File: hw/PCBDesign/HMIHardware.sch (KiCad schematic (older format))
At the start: 8 parts, among them U1 74HC165, U2 74HC165, U3 74HC165

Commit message: Added PCB
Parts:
- added R45, R46, R47, R49, R51: 10k, Resistor_SMD:R_0402_1005Metric, symbol Device:R_US
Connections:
- net GND: now also R45.2, R46.2, R47.2, R49.2, R51.2
- net d22: now also R45.1
- net d4: now also R46.1
- net d5: now also R47.1
- net d6: now also R49.1
- net d7: now also R51.1
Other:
- moved on the sheet: R2
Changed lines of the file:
@@
 F1 "ButtonInput.sch" 50
 F2 "V+" I L 9600 1750 50
-F3 "KeyLeft" O L 9600 1900 50
-F4 "KeyRight" O L 9600 2000 50
-F5 "KeyUp" O L 9600 2100 50
-F6 "KeyDown" O L 9600 2200 50
-F7 "KeyEnter" O L 9600 2300 50
-F8 "KeyEscape" O L 9600 2400 50
-F9 "KeyReset" O L 9600 2500 50
-F10 "KeyBoot" O L 9600 2600 50
+F3 "KeyReset" O L 9600 2500 50
+F4 "KeyBoot" O L 9600 2000 50
+F5 "KeyUser" O L 9600 1900 50
 $EndSheet
 Text HLabel 9550 6000 0    50   Input ~ 0
@@
 Wire Wire Line
 	9600 2000 9200 2000
-Wire Wire Line
-	9600 2100 9200 2100
-Wire Wire Line
-	9600 2200 9200 2200
-Wire Wire Line
-	9600 2300 9200 2300
-Wire Wire Line
-	9600 2400 9200 2400
 Wire Bus Line
 	7250 2800 9100 2800
@@
 Entry Wire Line
 	9100 1900 9200 2000
-Entry Wire Line
-	9100 2000 9200 2100
-Entry Wire Line
-	9100 2100 9200 2200
-Entry Wire Line
-	9100 2200 9200 2300
-Entry Wire Line
-	9100 2300 9200 2400
 Text Label 7000 2000 0    50   ~ 0
 d0
@@
 Text Label 9300 2000 0    50   ~ 0
 d3
-Text Label 9300 2100 0    50   ~ 0
-d4
-Text Label 9300 2200 0    50   ~ 0
-d5
-Text Label 9300 2300 0    50   ~ 0
-d6
-Text Label 9300 2400 0    50   ~ 0
-d7
 Wire Wire Line
 	4900 2000 5100 2000
@@
 L Device:R_US R2
 U 1 1 60588674
-P 8400 4650
-F 0 "R2" H 8468 4696 50  0000 L CNN
-F 1 "10k" H 8468 4605 50  0000 L CNN
-F 2 "Resistor_SMD:R_0402_1005Metric" V 8440 4640 50  0001 C CNN
-F 3 "~" H 8400 4650 50  0001 C CNN
-F 4 "C25744" H 8400 4650 50  0001 C CNN "LCSC"
-	1    8400 4650
+P 5250 4650
+F 0 "R2" H 5318 4696 50  0000 L CNN
+F 1 "10k" H 5318 4605 50  0000 L CNN
+F 2 "Resistor_SMD:R_0402_1005Metric" V 5290 4640 50  0001 C CNN
+F 3 "~" H 5250 4650 50  0001 C CNN
+F 4 "C25744" H 5250 4650 50  0001 C CNN "LCSC"
+	1    5250 4650
 	1    0    0    -1
 $EndComp
@@
 L power:GND #PWR020
 U 1 1 60589A9A
-P 8400 4800
-F 0 "#PWR020" H 8400 4550 50  0001 C CNN
-F 1 "GND" H 8405 4627 50  0000 C CNN
-F 2 "" H 8400 4800 50  0001 C CNN
-F 3 "" H 8400 4800 50  0001 C CNN
-	1    8400 4800
-	1    0    0    -1
-$EndComp
-Entry Wire Line
-	7400 4250 7500 4350
-Entry Wire Line
-	7700 4250 7800 4350
-Entry Wire Line
-	8000 4250 8100 4350
-Entry Wire Line
-	8300 4250 8400 4350
-Wire Wire Line
-	8400 4500 8400 4350
-Wire Wire Line
-	7800 4500 7800 4350
-Wire Wire Line
-	7500 4500 7500 4350
-Text Label 7500 4400 0    50   ~ 0
+P 5250 4800
+F 0 "#PWR020" H 5250 4550 50  0001 C CNN
+F 1 "GND" H 5255 4627 50  0000 C CNN
+F 2 "" H 5250 4800 50  0001 C CNN
+F 3 "" H 5250 4800 50  0001 C CNN
+	1    5250 4800
+	1    0    0    -1
+$EndComp
+Entry Wire Line
+	4250 4250 4350 4350
+Entry Wire Line
+	4550 4250 4650 4350
+Entry Wire Line
+	4850 4250 4950 4350
+Entry Wire Line
+	5150 4250 5250 4350
+Wire Wire Line
+	5250 4500 5250 4350
+Wire Wire Line
+	4650 4500 4650 4350
+Wire Wire Line
+	4350 4500 4350 4350
+Text Label 4350 4400 0    50   ~ 0
 d20
-Text Label 7800 4400 0    50   ~ 0
+Text Label 4650 4400 0    50   ~ 0
 d21
-Text Label 8100 4400 0    50   ~ 0
+Text Label 4950 4400 0    50   ~ 0
 d22
-Text Label 8400 4400 0    50   ~ 0
+Text Label 5250 4400 0    50   ~ 0
 d23
-Text Notes 8700 5550 1    50   ~ 0
+Text Notes 6300 5150 2    50   ~ 0
 These inputs currently unused
-Text GLabel 7500 4500 3    50   Output ~ 0
+Text GLabel 4350 4500 3    50   Output ~ 0
 nBatteryPowerGood
-Text GLabel 7800 4500 3    50   Output ~ 0
+Text GLabel 4650 4500 3    50   Output ~ 0
 nBatteryChargeGood
-Wire Wire Line
-	9200 2600 9600 2600
-Text Label 9200 2600 0    50   ~ 0
-nBoot
-Wire Wire Line
-	8100 4350 8100 4900
+$Comp
+L Device:R_US R45
+U 1 1 604B372E
+P 4950 4650
+F 0 "R45" H 5018 4696 50  0000 L CNN
+F 1 "10k" H 5018 4605 50  0000 L CNN
+F 2 "Resistor_SMD:R_0402_1005Metric" V 4990 4640 50  0001 C CNN
+F 3 "~" H 4950 4650 50  0001 C CNN
+F 4 "C25744" H 4950 4650 50  0001 C CNN "LCSC"
+	1    4950 4650
+	1    0    0    -1
+$EndComp
+$Comp
+L power:GND #PWR056
+U 1 1 604B3734
+P 4950 4800
+F 0 "#PWR056" H 4950 4550 50  0001 C CNN
+F 1 "GND" H 4955 4627 50  0000 C CNN
+F 2 "" H 4950 4800 50  0001 C CNN
+F 3 "" H 4950 4800 50  0001 C CNN
+	1    4950 4800
+	1    0    0    -1
+$EndComp
+Wire Wire Line
+	4950 4500 4950 4350
+$Comp
+L Device:R_US R46
+U 1 1 604BF334
+P 5550 4650
+F 0 "R46" H 5618 4696 50  0000 L CNN
+F 1 "10k" H 5618 4605 50  0000 L CNN
+F 2 "Resistor_SMD:R_0402_1005Metric" V 5590 4640 50  0001 C CNN
+F 3 "~" H 5550 4650 50  0001 C CNN
+F 4 "C25744" H 5550 4650 50  0001 C CNN "LCSC"
+	1    5550 4650
+	1    0    0    -1
+$EndComp
+$Comp
+L power:GND #PWR057
+U 1 1 604BF33A
+P 5550 4800
+F 0 "#PWR057" H 5550 4550 50  0001 C CNN
+F 1 "GND" H 5555 4627 50  0000 C CNN
+F 2 "" H 5550 4800 50  0001 C CNN
+F 3 "" H 5550 4800 50  0001 C CNN
+	1    5550 4800
+	1    0    0    -1
+$EndComp
+Entry Wire Line
+	5450 4250 5550 4350
+Wire Wire Line
+	5550 4500 5550 4350
+Text Label 5550 4400 0    50   ~ 0
+d4
+$Comp
+L Device:R_US R47
+U 1 1 604C2A2C
+P 5850 4650
+F 0 "R47" H 5918 4696 50  0000 L CNN
+F 1 "10k" H 5918 4605 50  0000 L CNN
+F 2 "Resistor_SMD:R_0402_1005Metric" V 5890 4640 50  0001 C CNN
+F 3 "~" H 5850 4650 50  0001 C CNN
+F 4 "C25744" H 5850 4650 50  0001 C CNN "LCSC"
+	1    5850 4650
+	1    0    0    -1
+$EndComp
+$Comp
+L power:GND #PWR058
+U 1 1 604C2A32
+P 5850 4800
+F 0 "#PWR058" H 5850 4550 50  0001 C CNN
+F 1 "GND" H 5855 4627 50  0000 C CNN
+F 2 "" H 5850 4800 50  0001 C CNN
+F 3 "" H 5850 4800 50  0001 C CNN
+	1    5850 4800
+	1    0    0    -1
+$EndComp
+Entry Wire Line
+	5750 4250 5850 4350
+Wire Wire Line
+	5850 4500 5850 4350
+Text Label 5850 4400 0    50   ~ 0
+d5
+$Comp
+L Device:R_US R49
+U 1 1 604C6290
+P 6150 4650
+F 0 "R49" H 6218 4696 50  0000 L CNN
+F 1 "10k" H 6218 4605 50  0000 L CNN
+F 2 "Resistor_SMD:R_0402_1005Metric" V 6190 4640 50  0001 C CNN
+F 3 "~" H 6150 4650 50  0001 C CNN
+F 4 "C25744" H 6150 4650 50  0001 C CNN "LCSC"
+	1    6150 4650
+	1    0    0    -1
+$EndComp
+$Comp
+L power:GND #PWR060
+U 1 1 604C6296
+P 6150 4800
+F 0 "#PWR060" H 6150 4550 50  0001 C CNN
+F 1 "GND" H 6155 4627 50  0000 C CNN
+F 2 "" H 6150 4800 50  0001 C CNN
+F 3 "" H 6150 4800 50  0001 C CNN
+	1    6150 4800
+	1    0    0    -1
+$EndComp
+Entry Wire Line
+	6050 4250 6150 4350
+Wire Wire Line
+	6150 4500 6150 4350
+Text Label 6150 4400 0    50   ~ 0
+d6
+$Comp
+L Device:R_US R51
+U 1 1 604C9E66
+P 6450 4650
+F 0 "R51" H 6518 4696 50  0000 L CNN
+F 1 "10k" H 6518 4605 50  0000 L CNN
+F 2 "Resistor_SMD:R_0402_1005Metric" V 6490 4640 50  0001 C CNN
+F 3 "~" H 6450 4650 50  0001 C CNN
+F 4 "C25744" H 6450 4650 50  0001 C CNN "LCSC"
+	1    6450 4650
+	1    0    0    -1
+$EndComp
+$Comp
+L power:GND #PWR062
+U 1 1 604C9E6C
+P 6450 4800
+F 0 "#PWR062" H 6450 4550 50  0001 C CNN
+F 1 "GND" H 6455 4627 50  0000 C CNN
+F 2 "" H 6450 4800 50  0001 C CNN
+F 3 "" H 6450 4800 50  0001 C CNN
+	1    6450 4800
+	1    0    0    -1
+$EndComp
+Entry Wire Line
+	6350 4250 6450 4350
+Wire Wire Line
+	6450 4500 6450 4350
+Text Label 6450 4400 0    50   ~ 0
+d7
 Wire Bus Line
 	9100 3950 9100 4250
 Wire Bus Line
+	9100 900  9100 2800
+Wire Bus Line
+	7250 2100 7250 2800
+Wire Bus Line
+	5200 2100 5200 2800
+Wire Bus Line
+	9100 3100 9100 3800
+Wire Bus Line
+	3000 2100 3000 2800
+Wire Bus Line
 	3500 4250 9100 4250
-Wire Bus Line
-	7250 2100 7250 2800
-Wire Bus Line
-	5200 2100 5200 2800
-Wire Bus Line
-	9100 3100 9100 3800
-Wire Bus Line
-	3000 2100 3000 2800
-Wire Bus Line
-	9100 900  9100 2800
-Text Label 8100 4900 1    50   ~ 0
-nBoot
 $EndSCHEMATC

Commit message: Lay out more PCB
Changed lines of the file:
@@
 Wire Wire Line
 	9600 2000 9200 2000
-Wire Bus Line
-	7250 2800 9100 2800
-Entry Wire Line
-	9100 900  9200 1000
-Entry Wire Line
-	9100 1000 9200 1100
-Entry Wire Line
-	9100 1800 9200 1900
-Entry Wire Line
-	9100 1900 9200 2000
 Text Label 7000 2000 0    50   ~ 0
 d0
@@
 Text Label 7000 2700 0    50   ~ 0
 d7
-Text Label 9300 1000 0    50   ~ 0
-d0
-Text Label 9300 1100 0    50   ~ 0
-d1
-Text Label 9300 1900 0    50   ~ 0
-d2
-Text Label 9300 2000 0    50   ~ 0
-d3
 Wire Wire Line
 	4900 2000 5100 2000
@@
 Entry Wire Line
 	9100 3800 9200 3900
-Wire Bus Line
-	5200 2800 5650 2800
 Text Label 4950 2000 0    50   ~ 0
 d8
@@
 Text Label 4950 2700 0    50   ~ 0
 d15
-Text Label 9300 3200 0    50   ~ 0
-d8
-Text Label 9300 3300 0    50   ~ 0
-d9
-Text Label 9300 3400 0    50   ~ 0
-d10
-Text Label 9300 3500 0    50   ~ 0
-d11
-Text Label 9300 3600 0    50   ~ 0
-d12
-Text Label 9300 3700 0    50   ~ 0
-d13
-Text Label 9300 3800 0    50   ~ 0
-d14
-Text Label 9300 3900 0    50   ~ 0
-d15
-Wire Bus Line
-	9100 3800 5650 3800
-Wire Bus Line
-	5650 2800 5650 3800
 Entry Wire Line
 	9100 3950 9200 4050
@@
 Entry Wire Line
 	9100 4250 9200 4350
-Text Label 9300 4050 0    50   ~ 0
-d16
-Text Label 9300 4150 0    50   ~ 0
-d17
-Text Label 9300 4250 0    50   ~ 0
-d18
-Text Label 9300 4350 0    50   ~ 0
-d19
 Wire Wire Line
 	2700 2000 2900 2000
@@
 Entry Wire Line
 	2900 2300 3000 2400
-Wire Bus Line
-	3000 2800 3500 2800
-Wire Bus Line
-	3500 2800 3500 4250
 Text Label 2750 2000 0    50   ~ 0
 d16
@@
 Wire Wire Line
 	4350 4500 4350 4350
-Text Label 4350 4400 0    50   ~ 0
-d20
-Text Label 4650 4400 0    50   ~ 0
-d21
-Text Label 4950 4400 0    50   ~ 0
-d22
-Text Label 5250 4400 0    50   ~ 0
-d23
 Text Notes 6300 5150 2    50   ~ 0
 These inputs currently unused
@@
 Wire Wire Line
 	5550 4500 5550 4350
-Text Label 5550 4400 0    50   ~ 0
-d4
 $Comp
 L Device:R_US R47
@@
 Wire Wire Line
 	5850 4500 5850 4350
-Text Label 5850 4400 0    50   ~ 0
-d5
 $Comp
 L Device:R_US R49
@@
 Wire Wire Line
 	6150 4500 6150 4350
-Text Label 6150 4400 0    50   ~ 0
-d6
 $Comp
 L Device:R_US R51
@@
 Wire Wire Line
 	6450 4500 6450 4350
-Text Label 6450 4400 0    50   ~ 0
-d7
-Wire Bus Line
-	9100 3950 9100 4250
-Wire Bus Line
-	9100 900  9100 2800
 Wire Bus Line
 	7250 2100 7250 2800
@@
 	5200 2100 5200 2800
 Wire Bus Line
-	9100 3100 9100 3800
-Wire Bus Line
 	3000 2100 3000 2800
-Wire Bus Line
-	3500 4250 9100 4250
 $EndSCHEMATC

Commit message: Complete route of draft #1 finished
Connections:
- wire segments 77 -> 75
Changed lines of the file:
@@
 Wire Wire Line
 	9500 2500 9600 2500
-Text HLabel 9500 4800 0    50   Input ~ 0
-VAnalogRef
 Wire Wire Line
 	9500 5050 9600 5050
@@
 Wire Wire Line
 	6950 2700 7150 2700
-Entry Wire Line
-	7150 2000 7250 2100
-Entry Wire Line
-	7150 2100 7250 2200
-Entry Wire Line
-	7150 2200 7250 2300
-Entry Wire Line
-	7150 2300 7250 2400
-Entry Wire Line
-	7150 2400 7250 2500
-Entry Wire Line
-	7150 2500 7250 2600
-Entry Wire Line
-	7150 2600 7250 2700
-Entry Wire Line
-	7150 2700 7250 2800
 Wire Wire Line
 	9600 1000 9200 1000
@@
 Wire Wire Line
 	4900 2700 5100 2700
-Entry Wire Line
-	5100 2000 5200 2100
-Entry Wire Line
-	5100 2100 5200 2200
-Entry Wire Line
-	5100 2200 5200 2300
-Entry Wire Line
-	5100 2300 5200 2400
-Entry Wire Line
-	5100 2400 5200 2500
-Entry Wire Line
-	5100 2500 5200 2600
-Entry Wire Line
-	5100 2600 5200 2700
-Entry Wire Line
-	5100 2700 5200 2800
 Wire Wire Line
 	9600 3200 9200 3200
@@
 Wire Wire Line
 	9600 4350 9200 4350
-Entry Wire Line
-	9100 3100 9200 3200
-Entry Wire Line
-	9100 3300 9200 3400
-Entry Wire Line
-	9100 3200 9200 3300
-Entry Wire Line
-	9100 3400 9200 3500
-Entry Wire Line
-	9100 3600 9200 3700
-Entry Wire Line
-	9100 3700 9200 3800
-Entry Wire Line
-	9100 3500 9200 3600
-Entry Wire Line
-	9100 3800 9200 3900
 Text Label 4950 2000 0    50   ~ 0
 d8
@@
 Text Label 4950 2700 0    50   ~ 0
 d15
-Entry Wire Line
-	9100 3950 9200 4050
-Entry Wire Line
-	9100 4050 9200 4150
-Entry Wire Line
-	9100 4150 9200 4250
-Entry Wire Line
-	9100 4250 9200 4350
 Wire Wire Line
 	2700 2000 2900 2000
@@
 Wire Wire Line
 	2700 2700 2900 2700
-Entry Wire Line
-	2900 2000 3000 2100
-Entry Wire Line
-	2900 2100 3000 2200
-Entry Wire Line
-	2900 2200 3000 2300
-Entry Wire Line
-	2900 2300 3000 2400
 Text Label 2750 2000 0    50   ~ 0
 d16
@@
 Text Label 2750 2700 0    50   ~ 0
 d23
-Entry Wire Line
-	2900 2700 3000 2800
-Entry Wire Line
-	2900 2600 3000 2700
-Entry Wire Line
-	2900 2500 3000 2600
-Entry Wire Line
-	2900 2400 3000 2500
 $Comp
 L Device:R_US R2
@@
 	1    0    0    -1
 $EndComp
-Entry Wire Line
-	4250 4250 4350 4350
-Entry Wire Line
-	4550 4250 4650 4350
-Entry Wire Line
-	4850 4250 4950 4350
-Entry Wire Line
-	5150 4250 5250 4350
 Wire Wire Line
 	5250 4500 5250 4350
-Wire Wire Line
-	4650 4500 4650 4350
-Wire Wire Line
-	4350 4500 4350 4350
 Text Notes 6300 5150 2    50   ~ 0
 These inputs currently unused
-Text GLabel 4350 4500 3    50   Output ~ 0
+Text GLabel 7150 2000 2    50   Output ~ 0
 nBatteryPowerGood
-Text GLabel 4650 4500 3    50   Output ~ 0
+Text GLabel 7150 2100 2    50   Output ~ 0
 nBatteryChargeGood
 $Comp
@@
 	1    0    0    -1
 $EndComp
-Entry Wire Line
-	5450 4250 5550 4350
 Wire Wire Line
 	5550 4500 5550 4350
@@
 	1    0    0    -1
 $EndComp
-Entry Wire Line
-	5750 4250 5850 4350
 Wire Wire Line
 	5850 4500 5850 4350
@@
 	1    0    0    -1
 $EndComp
-Entry Wire Line
-	6050 4250 6150 4350
 Wire Wire Line
 	6150 4500 6150 4350
@@
 	1    0    0    -1
 $EndComp
-Entry Wire Line
-	6350 4250 6450 4350
 Wire Wire Line
 	6450 4500 6450 4350
-Wire Bus Line
-	7250 2100 7250 2800
-Wire Bus Line
-	5200 2100 5200 2800
-Wire Bus Line
-	3000 2100 3000 2800
+Text Label 9250 1000 0    50   ~ 0
+d7
+Text Label 9250 1100 0    50   ~ 0
+d6
+Text Label 9250 2000 0    50   ~ 0
+d5
+Text Label 9250 1900 0    50   ~ 0
+d4
+Text Label 9300 4350 0    50   ~ 0
+d2
+Text HLabel 9500 4800 0    50   Input ~ 0
+VAnalogRef
+Text Label 9300 3400 0    50   ~ 0
+d3
+Text Label 9300 3500 0    50   ~ 0
+d15
+Text Label 9300 3200 0    50   ~ 0
+d14
+Text Label 9300 4250 0    50   ~ 0
+d13
+Text Label 9300 3300 0    50   ~ 0
+d12
+Text Label 9300 3600 0    50   ~ 0
+d8
+Text Label 9300 4150 0    50   ~ 0
+d9
+Text Label 9300 3700 0    50   ~ 0
+d10
+Text Label 9300 3800 0    50   ~ 0
+d11
+Text Label 9300 4050 0    50   ~ 0
+d23
+Text Label 9300 3900 0    50   ~ 0
+d22
+Text Label 6450 4350 0    50   ~ 0
+d19
+Text Label 5850 4350 0    50   ~ 0
+d18
+Text Label 5250 4350 0    50   ~ 0
+d17
+Text Label 6150 4350 0    50   ~ 0
+d16
+Text Label 4950 4350 0    50   ~ 0
+d21
+Text Label 5550 4350 0    50   ~ 0
+d20
 $EndSCHEMATC

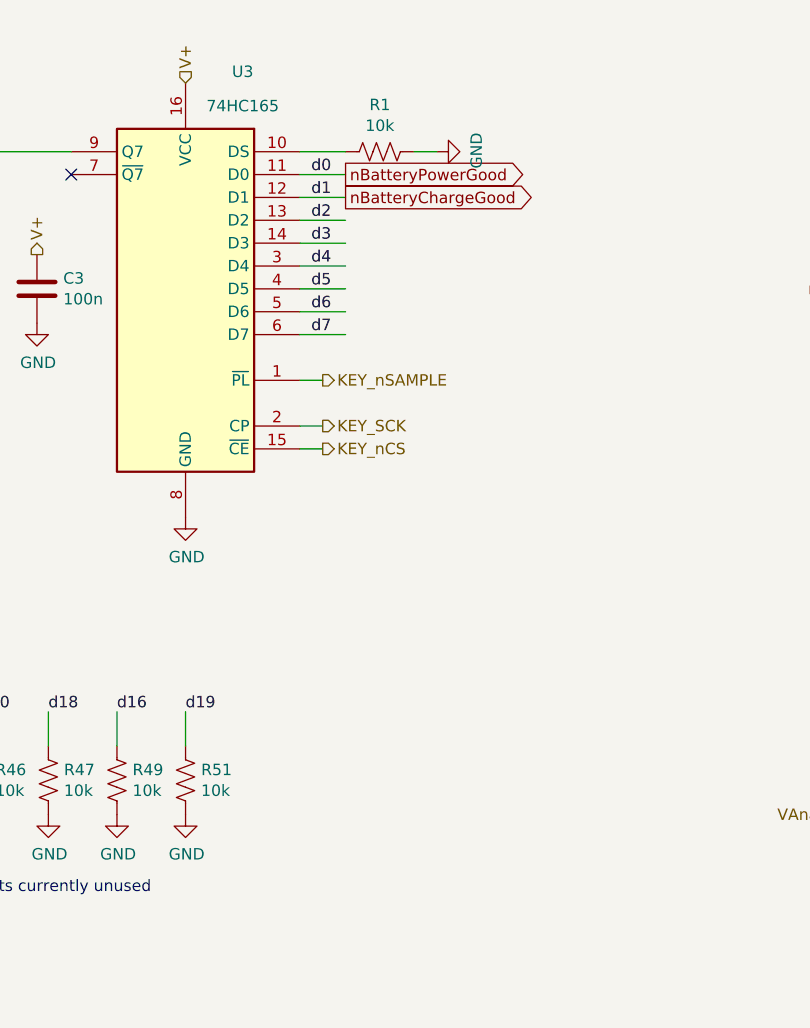
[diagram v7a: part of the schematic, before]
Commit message: Start working on PCB rev 2.0
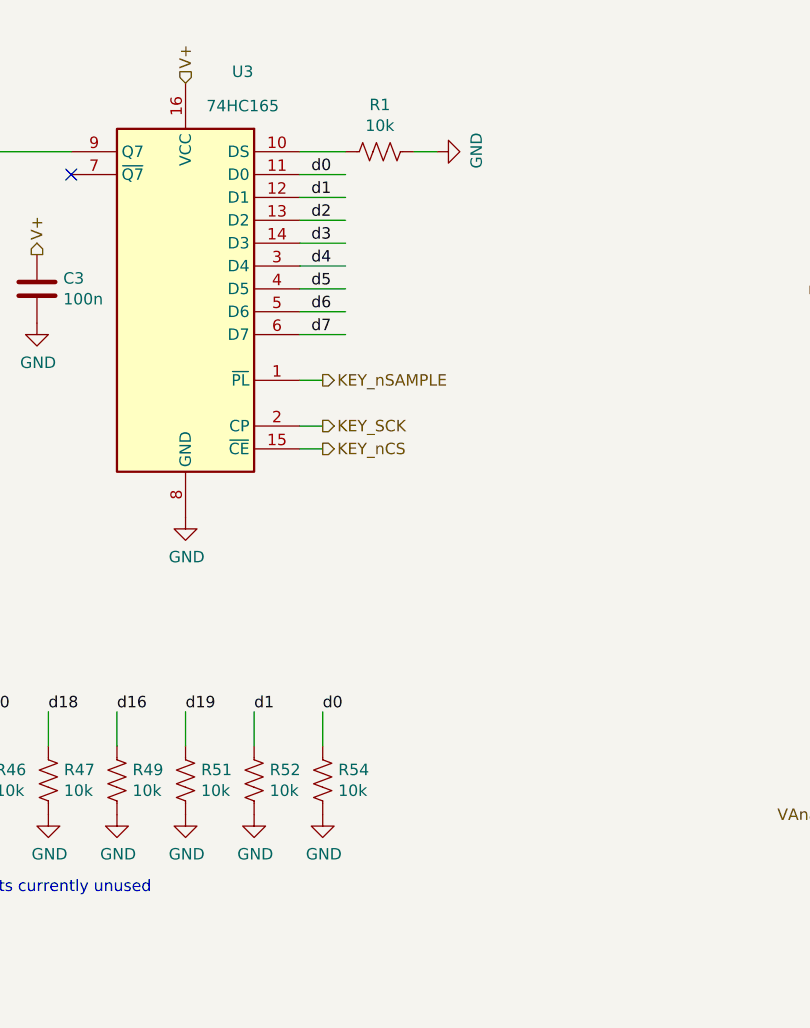
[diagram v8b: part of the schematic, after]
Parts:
- added R52, R54: 10k, Resistor_SMD:R_0402_1005Metric, symbol Device:R_US
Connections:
- net labels removed: nBatteryChargeGood, nBatteryPowerGood
- wire segments 75 -> 77
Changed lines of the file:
@@
 Text Notes 6300 5150 2    50   ~ 0
 These inputs currently unused
-Text GLabel 7150 2000 2    50   Output ~ 0
-nBatteryPowerGood
-Text GLabel 7150 2100 2    50   Output ~ 0
-nBatteryChargeGood
 $Comp
 L Device:R_US R45
@@
 Text Label 5550 4350 0    50   ~ 0
 d20
+$Comp
+L Device:R_US R52
+U 1 1 61E28C24
+P 6750 4650
+F 0 "R52" H 6818 4696 50  0000 L CNN
+F 1 "10k" H 6818 4605 50  0000 L CNN
+F 2 "Resistor_SMD:R_0402_1005Metric" V 6790 4640 50  0001 C CNN
+F 3 "~" H 6750 4650 50  0001 C CNN
+F 4 "C25744" H 6750 4650 50  0001 C CNN "LCSC"
+	1    6750 4650
+	1    0    0    -1
+$EndComp
+$Comp
+L power:GND #PWR071
+U 1 1 61E28C2A
+P 6750 4800
+F 0 "#PWR071" H 6750 4550 50  0001 C CNN
+F 1 "GND" H 6755 4627 50  0000 C CNN
+F 2 "" H 6750 4800 50  0001 C CNN
+F 3 "" H 6750 4800 50  0001 C CNN
+	1    6750 4800
+	1    0    0    -1
+$EndComp
+Wire Wire Line
+	6750 4500 6750 4350
+$Comp
+L Device:R_US R54
+U 1 1 61E28C32
+P 7050 4650
+F 0 "R54" H 7118 4696 50  0000 L CNN
+F 1 "10k" H 7118 4605 50  0000 L CNN
+F 2 "Resistor_SMD:R_0402_1005Metric" V 7090 4640 50  0001 C CNN
+F 3 "~" H 7050 4650 50  0001 C CNN
+F 4 "C25744" H 7050 4650 50  0001 C CNN "LCSC"
+	1    7050 4650
+	1    0    0    -1
+$EndComp
+$Comp
+L power:GND #PWR079
+U 1 1 61E28C38
+P 7050 4800
+F 0 "#PWR079" H 7050 4550 50  0001 C CNN
+F 1 "GND" H 7055 4627 50  0000 C CNN
+F 2 "" H 7050 4800 50  0001 C CNN
+F 3 "" H 7050 4800 50  0001 C CNN
+	1    7050 4800
+	1    0    0    -1
+$EndComp
+Wire Wire Line
+	7050 4500 7050 4350
+Text Label 7050 4350 0    50   ~ 0
+d0
+Text Label 6750 4350 0    50   ~ 0
+d1
 $EndSCHEMATC
